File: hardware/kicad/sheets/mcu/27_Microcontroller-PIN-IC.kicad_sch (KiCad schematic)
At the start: 19 parts, among them U141 PCAL6524HEAZ

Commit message: reorganized
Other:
- title: Microcontroller-PIN-IC -> MCU GPIO Expander
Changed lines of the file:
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@@
 	(paper "User" 297 210)
 	(title_block
-		(title "Microcontroller-PIN-IC")
+		(title "MCU GPIO Expander")
 		(date "2026-02-16")
 	)

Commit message: before final cleanup
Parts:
- renumbered C241 to C44, R472 to R76, R474 to R77, R475 to R78, R505 to R79, R506 to R80, R485 to R81, R480 to R82, R507 to R83, R496 to R84, R508 to R85, R501 to R86, R504 to R87, R443 to R88, U141 to U12, U160 to U13, U161 to U14, U159 to U15, U158 to U16

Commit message: clearer power path with sheets
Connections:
- net MCU-TPS-SHDN# renamed MCU-TPS-SHDN
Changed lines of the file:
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@@
 		)
 	)
-	(global_label "MCU-TPS-SHDN#"
+	(global_label "MCU-TPS-SHDN"
 		(shape output)
 		(at 273.05 95.25 0)

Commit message: more sheet simplfiication and pre simpler 12v sym
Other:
- moved on the sheet: C44, R76, R77, R78, R79, R80, R81, R82, R83, R84, R85, R86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

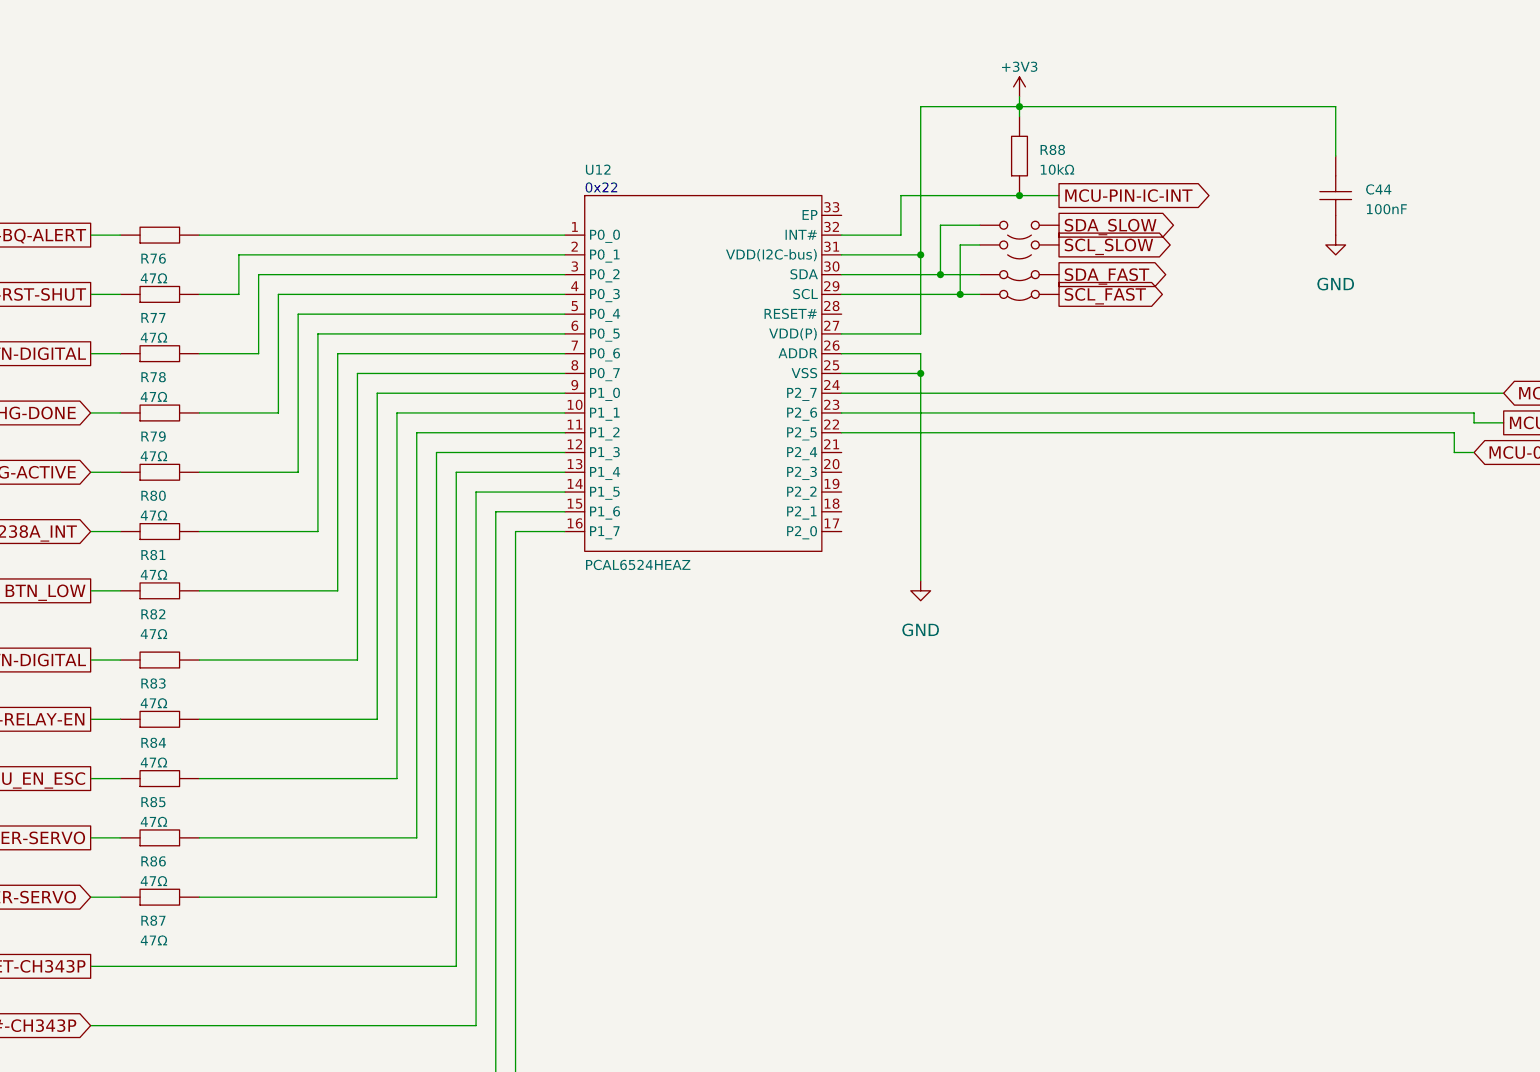
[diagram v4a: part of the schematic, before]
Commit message: resheeted bms and fixed links for the 12v buck
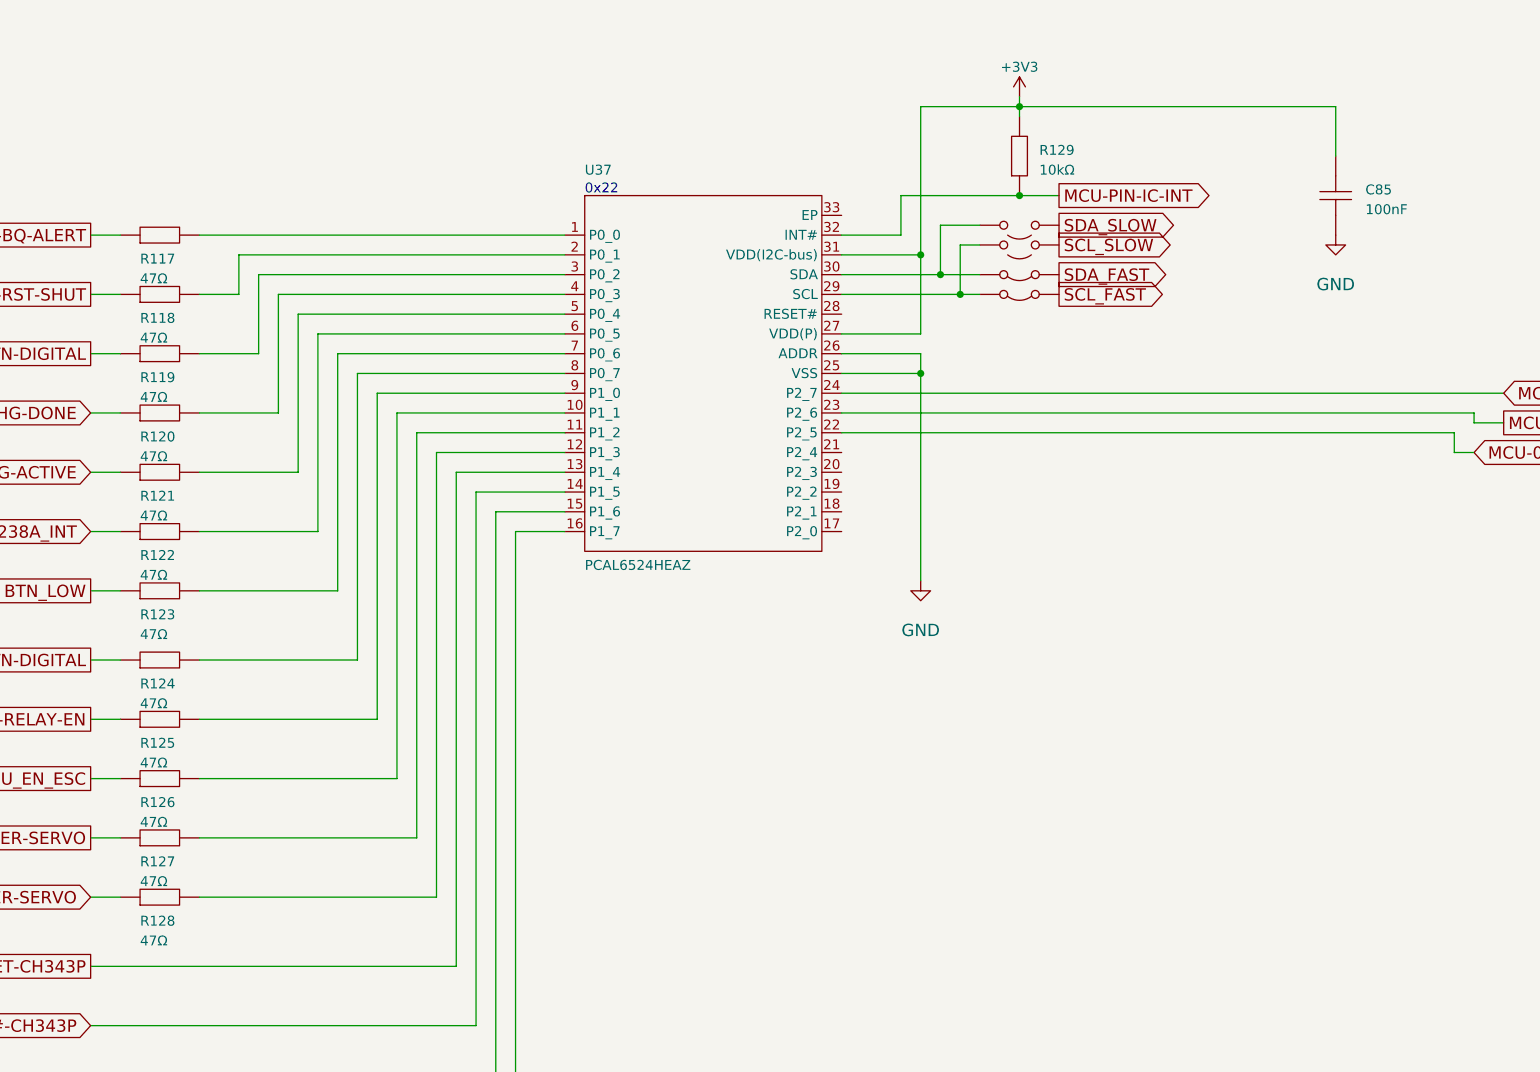
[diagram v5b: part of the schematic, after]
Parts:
- renumbered C44 to C85, R76 to R117, R77 to R118, R78 to R119, R79 to R120, R80 to R121, R81 to R122, R82 to R123, R83 to R124, R84 to R125, R85 to R126, R86 to R127, R87 to R128, R88 to R129, U12 to U37, U13 to U38, U14 to U39, U15 to U40, U16 to U41
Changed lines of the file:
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@@
 		(on_board yes)
 		(dnp no)
-		(property "Reference" "R81"
+		(property "Reference" "R122"
 			(at 69.85 99.06 0)
 			(effects
@@
 			(project "svea_powerboard_rev3"
 				(path "/3f85abf4-0b95-4c4a-b7e9-06f59ca1ea3d/5c2e021f-c2d4-49e2-8c36-9a64f1f12004/8d05c3b8-20a4-4a7f-9b20-01f8d5d5be42"
-					(reference "R81")
+					(reference "R122")
 					(unit 1)
 				)
@@
 		(on_board yes)
 		(dnp no)
-		(property "Reference" "R80"
+		(property "Reference" "R121"
 			(at 69.85 91.44 0)
 			(effects
@@
 			(project "svea_powerboard_rev3"
 				(path "/3f85abf4-0b95-4c4a-b7e9-06f59ca1ea3d/5c2e021f-c2d4-49e2-8c36-9a64f1f12004/8d05c3b8-20a4-4a7f-9b20-01f8d5d5be42"
-					(reference "R80")
+					(reference "R121")
 					(unit 1)
 				)
@@
 		(on_board yes)
 		(dnp no)
-		(property "Reference" "U15"
+		(property "Reference" "U40"
 			(at 182.88 62.23 0)
 			(effects
@@
 			(project "svea_powerboard_rev3"
 				(path "/3f85abf4-0b95-4c4a-b7e9-06f59ca1ea3d/5c2e021f-c2d4-49e2-8c36-9a64f1f12004/8d05c3b8-20a4-4a7f-9b20-01f8d5d5be42"
-					(reference "U15")
+					(reference "U40")
 					(unit 1)
 				)
@@
 		(on_board yes)
 		(dnp no)
-		(property "Reference" "C44"
+		(property "Reference" "C85"
 			(at 227.33 52.07 90)
 			(effects
@@
 			(project "svea_powerboard_rev3"
 				(path "/3f85abf4-0b95-4c4a-b7e9-06f59ca1ea3d/5c2e021f-c2d4-49e2-8c36-9a64f1f12004/8d05c3b8-20a4-4a7f-9b20-01f8d5d5be42"
-					(reference "C44")
+					(reference "C85")
 					(unit 1)
 				)
@@
 		(on_board yes)
 		(dnp no)
-		(property "Reference" "#PWR0155"
+		(property "Reference" "#PWR0115"
 			(at 223.52 57.15 0)
 			(effects
@@
 			(project "svea_powerboard_rev3"
 				(path "/3f85abf4-0b95-4c4a-b7e9-06f59ca1ea3d/5c2e021f-c2d4-49e2-8c36-9a64f1f12004/8d05c3b8-20a4-4a7f-9b20-01f8d5d5be42"
-					(reference "#PWR0155")
+					(reference "#PWR0115")
 					(unit 1)
 				)
@@
 		(on_board yes)
 		(dnp no)
-		(property "Reference" "R79"
+		(property "Reference" "R120"
 			(at 69.85 83.82 0)
 			(effects
@@
 			(project "svea_powerboard_rev3"
 				(path "/3f85abf4-0b95-4c4a-b7e9-06f59ca1ea3d/5c2e021f-c2d4-49e2-8c36-9a64f1f12004/8d05c3b8-20a4-4a7f-9b20-01f8d5d5be42"
-					(reference "R79")
+					(reference "R120")
 					(unit 1)
 				)
@@
 		(on_board yes)
 		(dnp no)
-		(property "Reference" "U14"
+		(property "Reference" "U39"
 			(at 180.34 57.15 0)
 			(effects
@@
 			(project "svea_powerboard_rev3"
 				(path "/3f85abf4-0b95-4c4a-b7e9-06f59ca1ea3d/5c2e021f-c2d4-49e2-8c36-9a64f1f12004/8d05c3b8-20a4-4a7f-9b20-01f8d5d5be42"
-					(reference "U14")
+					(reference "U39")
 					(unit 1)
 				)
@@
 		(on_board yes)
 		(dnp no)
-		(property "Reference" "R77"
+		(property "Reference" "R118"
 			(at 69.85 68.58 0)
 			(effects
@@
 			(project "svea_powerboard_rev3"
 				(path "/3f85abf4-0b95-4c4a-b7e9-06f59ca1ea3d/5c2e021f-c2d4-49e2-8c36-9a64f1f12004/8d05c3b8-20a4-4a7f-9b20-01f8d5d5be42"
-					(reference "R77")
+					(reference "R118")
 					(unit 1)
 				)
@@
 		(on_board yes)
 		(dnp no)
-		(property "Reference" "R84"
+		(property "Reference" "R125"
 			(at 69.85 123.19 0)
 			(effects
@@
 			(project "svea_powerboard_rev3"
 				(path "/3f85abf4-0b95-4c4a-b7e9-06f59ca1ea3d/5c2e021f-c2d4-49e2-8c36-9a64f1f12004/8d05c3b8-20a4-4a7f-9b20-01f8d5d5be42"
-					(reference "R84")
+					(reference "R125")
 					(unit 1)
 				)
@@
 		(on_board yes)
 		(dnp no)
-		(property "Reference" "U12"
+		(property "Reference" "U37"
 			(at 127 49.53 0)
 			(effects
@@
 			(project "svea_powerboard_rev3"
 				(path "/3f85abf4-0b95-4c4a-b7e9-06f59ca1ea3d/5c2e021f-c2d4-49e2-8c36-9a64f1f12004/8d05c3b8-20a4-4a7f-9b20-01f8d5d5be42"
-					(reference "U12")
+					(reference "U37")
 					(unit 1)
 				)
@@
 		(on_board yes)
 		(dnp no)
-		(property "Reference" "R82"
+		(property "Reference" "R123"
 			(at 69.85 106.68 0)
 			(effects
@@
 			(project "svea_powerboard_rev3"
 				(path "/3f85abf4-0b95-4c4a-b7e9-06f59ca1ea3d/5c2e021f-c2d4-49e2-8c36-9a64f1f12004/8d05c3b8-20a4-4a7f-9b20-01f8d5d5be42"
-					(reference "R82")
+					(reference "R123")
 					(unit 1)
 				)
@@
 		(on_board yes)
 		(dnp no)
-		(property "Reference" "U13"
+		(property "Reference" "U38"
 			(at 180.34 54.61 0)
 			(effects
@@
 			(project "svea_powerboard_rev3"
 				(path "/3f85abf4-0b95-4c4a-b7e9-06f59ca1ea3d/5c2e021f-c2d4-49e2-8c36-9a64f1f12004/8d05c3b8-20a4-4a7f-9b20-01f8d5d5be42"
-					(reference "U13")
+					(reference "U38")
 					(unit 1)
 				)
@@
 		(on_board yes)
 		(dnp no)
-		(property "Reference" "R78"
+		(property "Reference" "R119"
 			(at 69.85 76.2 0)
 			(effects
@@
 			(project "svea_powerboard_rev3"
 				(path "/3f85abf4-0b95-4c4a-b7e9-06f59ca1ea3d/5c2e021f-c2d4-49e2-8c36-9a64f1f12004/8d05c3b8-20a4-4a7f-9b20-01f8d5d5be42"
-					(reference "R78")
+					(reference "R119")
 					(unit 1)
 				)
@@
 		(on_board yes)
 		(dnp no)
-		(property "Reference" "R88"
+		(property "Reference" "R129"
 			(at 185.42 46.99 90)
 			(effects
@@
 			(project "svea_powerboard_rev3"
 				(path "/3f85abf4-0b95-4c4a-b7e9-06f59ca1ea3d/5c2e021f-c2d4-49e2-8c36-9a64f1f12004/8d05c3b8-20a4-4a7f-9b20-01f8d5d5be42"
-					(reference "R88")
+					(reference "R129")
 					(unit 1)
 				)
@@
 		(on_board yes)
 		(dnp no)
-		(property "Reference" "R87"
+		(property "Reference" "R128"
 			(at 69.85 146.05 0)
 			(effects
@@
 			(project "svea_powerboard_rev3"
 				(path "/3f85abf4-0b95-4c4a-b7e9-06f59ca1ea3d/5c2e021f-c2d4-49e2-8c36-9a64f1f12004/8d05c3b8-20a4-4a7f-9b20-01f8d5d5be42"
-					(reference "R87")
+					(reference "R128")
 					(unit 1)
 				)
@@
 		(on_board yes)
 		(dnp no)
-		(property "Reference" "R86"
+		(property "Reference" "R127"
 			(at 69.85 138.43 0)
 			(effects
@@
 			(project "svea_powerboard_rev3"
 				(path "/3f85abf4-0b95-4c4a-b7e9-06f59ca1ea3d/5c2e021f-c2d4-49e2-8c36-9a64f1f12004/8d05c3b8-20a4-4a7f-9b20-01f8d5d5be42"
-					(reference "R86")
+					(reference "R127")
 					(unit 1)
 				)
@@
 		(on_board yes)
 		(dnp no)
-		(property "Reference" "U16"
+		(property "Reference" "U41"
 			(at 182.88 64.77 0)
 			(effects
@@
 			(project "svea_powerboard_rev3"
 				(path "/3f85abf4-0b95-4c4a-b7e9-06f59ca1ea3d/5c2e021f-c2d4-49e2-8c36-9a64f1f12004/8d05c3b8-20a4-4a7f-9b20-01f8d5d5be42"
-					(reference "U16")
+					(reference "U41")
 					(unit 1)
 				)
@@
 		(on_board yes)
 		(dnp no)
-		(property "Reference" "#PWR0154"
+		(property "Reference" "#PWR0114"
 			(at 182.88 39.37 0)
 			(effects
@@
 			(project "svea_powerboard_rev3"
 				(path "/3f85abf4-0b95-4c4a-b7e9-06f59ca1ea3d/5c2e021f-c2d4-49e2-8c36-9a64f1f12004/8d05c3b8-20a4-4a7f-9b20-01f8d5d5be42"
-					(reference "#PWR0154")
+					(reference "#PWR0114")
 					(unit 1)
 				)
@@
 		(on_board yes)
 		(dnp no)
-		(property "Reference" "R76"
+		(property "Reference" "R117"
 			(at 69.85 60.96 0)
 			(effects
@@
 			(project "svea_powerboard_rev3"
 				(path "/3f85abf4-0b95-4c4a-b7e9-06f59ca1ea3d/5c2e021f-c2d4-49e2-8c36-9a64f1f12004/8d05c3b8-20a4-4a7f-9b20-01f8d5d5be42"
-					(reference "R76")
+					(reference "R117")
 					(unit 1)
 				)
@@
 		(on_board yes)
 		(dnp no)
-		(property "Reference" "R83"
+		(property "Reference" "R124"
 			(at 69.85 115.57 0)
 			(effects
@@
 			(project "svea_powerboard_rev3"
 				(path "/3f85abf4-0b95-4c4a-b7e9-06f59ca1ea3d/5c2e021f-c2d4-49e2-8c36-9a64f1f12004/8d05c3b8-20a4-4a7f-9b20-01f8d5d5be42"
-					(reference "R83")
+					(reference "R124")
 					(unit 1)
 				)
@@
 		(on_board yes)
 		(dnp no)
-		(property "Reference" "R85"
+		(property "Reference" "R126"
 			(at 69.85 130.81 0)
 			(effects
@@
 			(project "svea_powerboard_rev3"
 				(path "/3f85abf4-0b95-4c4a-b7e9-06f59ca1ea3d/5c2e021f-c2d4-49e2-8c36-9a64f1f12004/8d05c3b8-20a4-4a7f-9b20-01f8d5d5be42"
-					(reference "R85")
+					(reference "R126")
 					(unit 1)
 				)
@@
 		(on_board yes)
 		(dnp no)
-		(property "Reference" "#PWR0156"
+		(property "Reference" "#PWR0113"
 			(at 170.18 101.6 0)
 			(effects
@@
 			(project "svea_powerboard_rev3"
 				(path "/3f85abf4-0b95-4c4a-b7e9-06f59ca1ea3d/5c2e021f-c2d4-49e2-8c36-9a64f1f12004/8d05c3b8-20a4-4a7f-9b20-01f8d5d5be42"
-					(reference "#PWR0156")
+					(reference "#PWR0113")
 					(unit 1)
 				)
